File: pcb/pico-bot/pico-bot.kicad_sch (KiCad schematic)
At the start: 27 parts

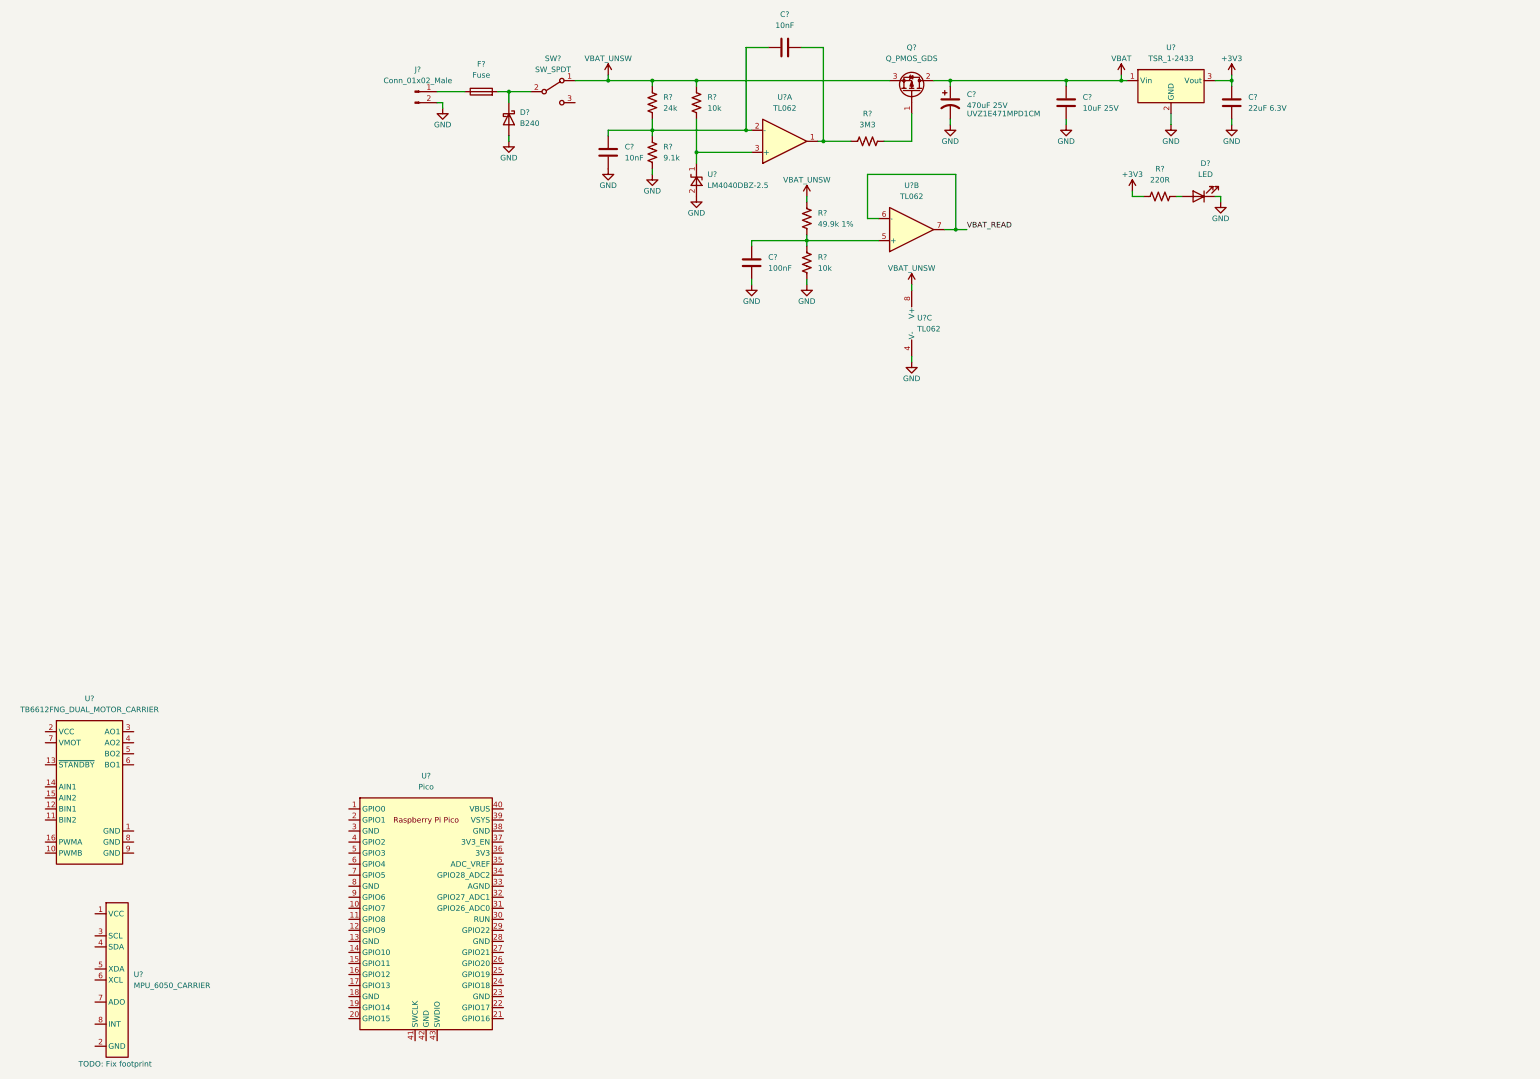
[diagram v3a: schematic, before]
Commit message: Add motor controller and imu circuits, create rpi pico w
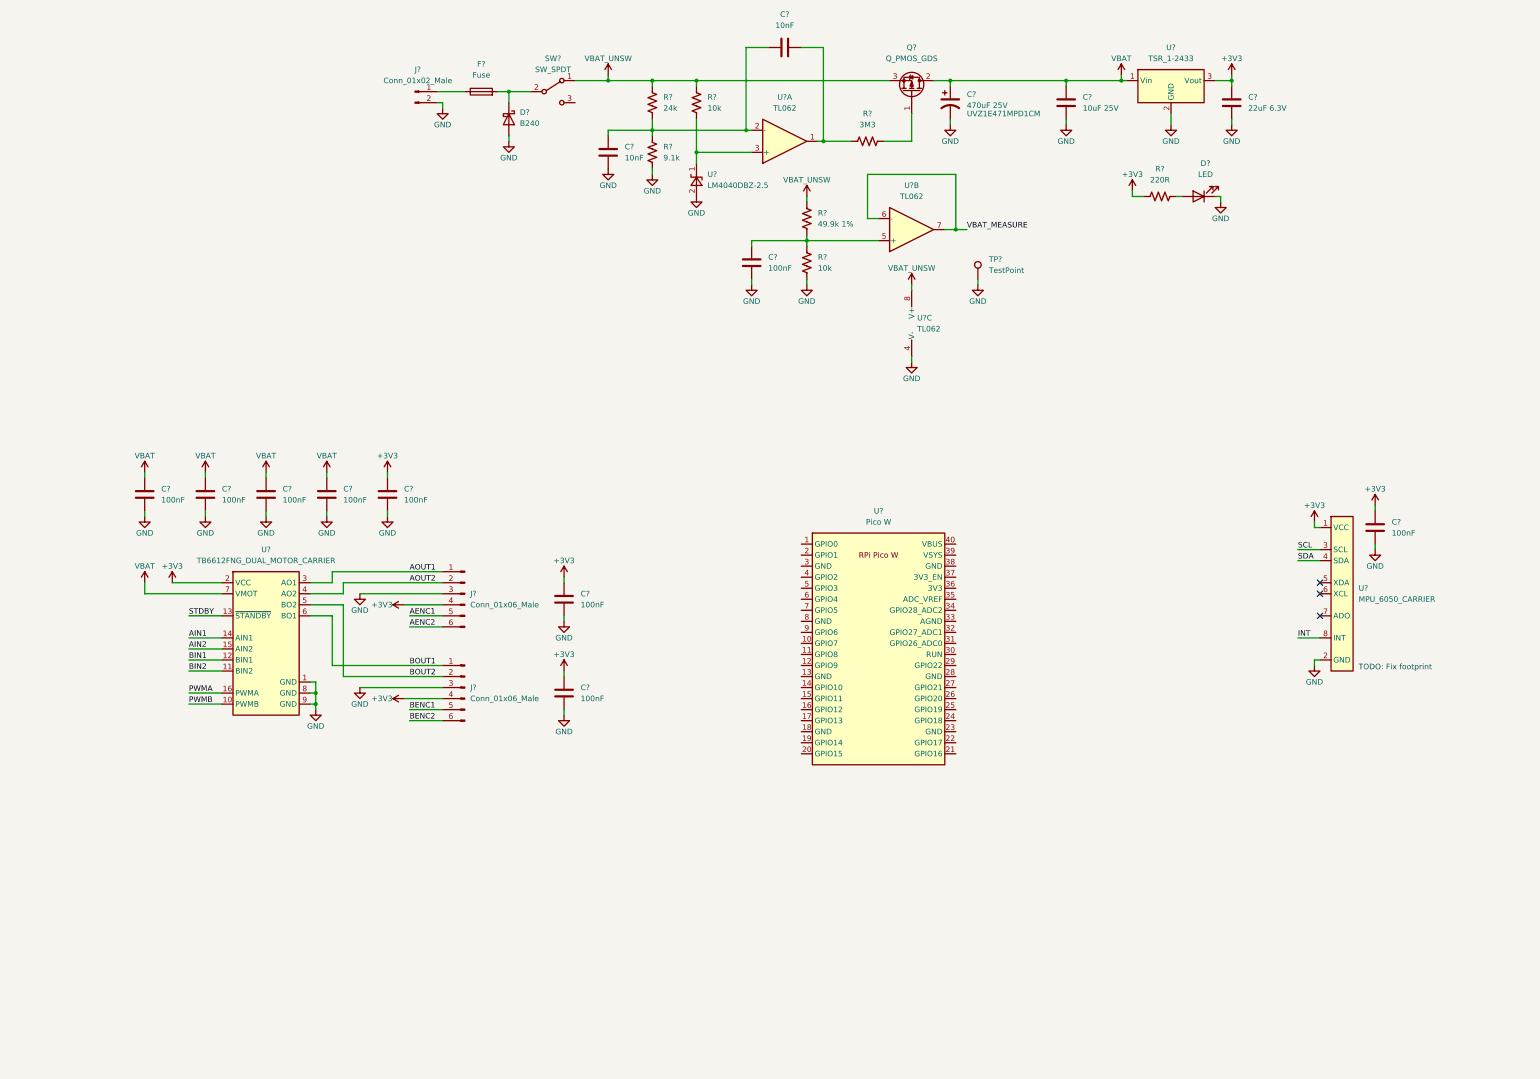
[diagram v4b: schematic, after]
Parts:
- removed U?: Pico, RPi_Pico:RPi_Pico_SMD_TH, symbol MCU_RaspberryPi_and_Boards:Pico
- added C? (x8): 100nF, Capacitor_SMD:C_0805_2012Metric_Pad1.18x1.45mm_HandSolder, symbol Device:C
- added J? (x2): Conn_01x06_Male, Connector_PinHeader_2.54mm:PinHeader_1x06_P2.54mm_Vertical, symbol Connector:Conn_01x06_Male
- added TP?: TestPoint, Connector_PinHeader_2.54mm:PinHeader_1x01_P2.54mm_Vertical, symbol Connector:TestPoint
- added U?: Pico W, RPi_Pico:RPi_Pico_SMD_TH, symbol pico-bot:Pico W
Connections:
- net +3V3: now also U?.1 (VCC), U?.2 (VCC), C?.2, C?.2, C?.2, C?.2, J?.4 (Pin_4), J?.4 (Pin_4)
- net GND: now also U?.1 (GND), U?.2 (GND), U?.8 (GND), U?.9 (GND), C?.1, C?.1, C?.1, C?.1, C?.1, C?.1, C?.1, C?.1, J?.3 (Pin_3), J?.3 (Pin_3), TP?.1
- net VBAT: now also U?.7 (VMOT), C?.2, C?.2, C?.2, C?.2
- net PWMB: now reaches U?.10 (PWMB)
- net BIN2: now reaches U?.11 (BIN2)
- net BIN1: now reaches U?.12 (BIN1)
- net STDBY: now reaches U?.13 (~{STANDBY})
- net AIN1: now reaches U?.14 (AIN1)
- net AIN2: now reaches U?.15 (AIN2)
- net PWMA: now reaches U?.16 (PWMA)
- net AOUT1: now reaches U?.3 (AO1)
- net AOUT1: now also J?.1 (Pin_1)
- net AOUT2: now reaches U?.4 (AO2)
- net AOUT2: now also J?.2 (Pin_2)
- net BOUT2: now reaches U?.5 (BO2)
- net BOUT2: now also J?.2 (Pin_2)
- net BOUT1: now reaches U?.6 (BO1)
- net BOUT1: now also J?.1 (Pin_1)
- net SCL: now reaches U?.3 (SCL)
- net SDA: now reaches U?.4 (SDA)
- net INT: now reaches U?.8 (INT)
- net VBAT_READ renamed VBAT_MEASURE
- new net AENC1: J?.5 (Pin_5)
- new net AENC2: J?.6 (Pin_6)
- new net BENC1: J?.5 (Pin_5)
- new net BENC2: J?.6 (Pin_6)
- no-connect marks 0 -> 3
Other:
- moved on the sheet: U?

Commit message: Progress commit
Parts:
- added Q?: DMG2305UX, symbol Device:Q_PMOS_DGS
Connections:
- net GND: now also U?.13 (GND), U?.18 (GND), U?.23 (GND), U?.28 (GND), U?.3 (GND), U?.33 (AGND), U?.38 (GND), U?.8 (GND)
- net INT: now also U?.11 (GPIO8)
- net SCL: now also U?.10 (GPIO7)
- net SDA: now also U?.9 (GPIO6)
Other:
- note added: "TODO: Check pins match footprint"
- moved on the sheet: C?, J?, U?

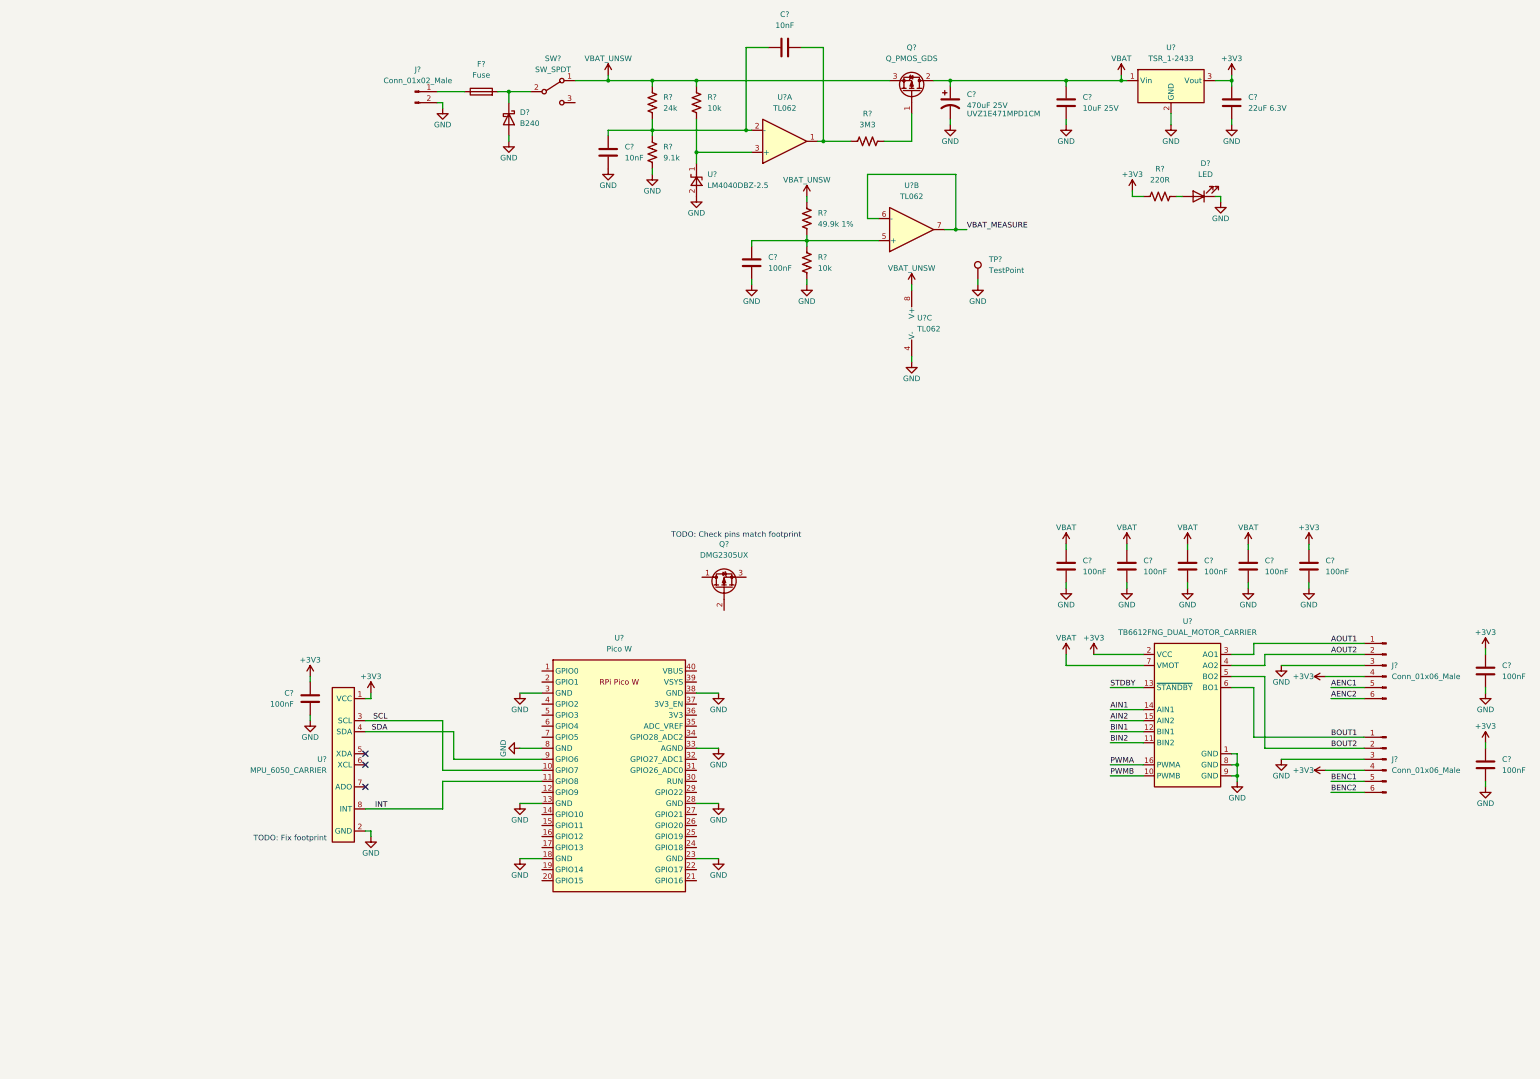
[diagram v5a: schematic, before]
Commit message: Add pico external power circuit, wire up pico
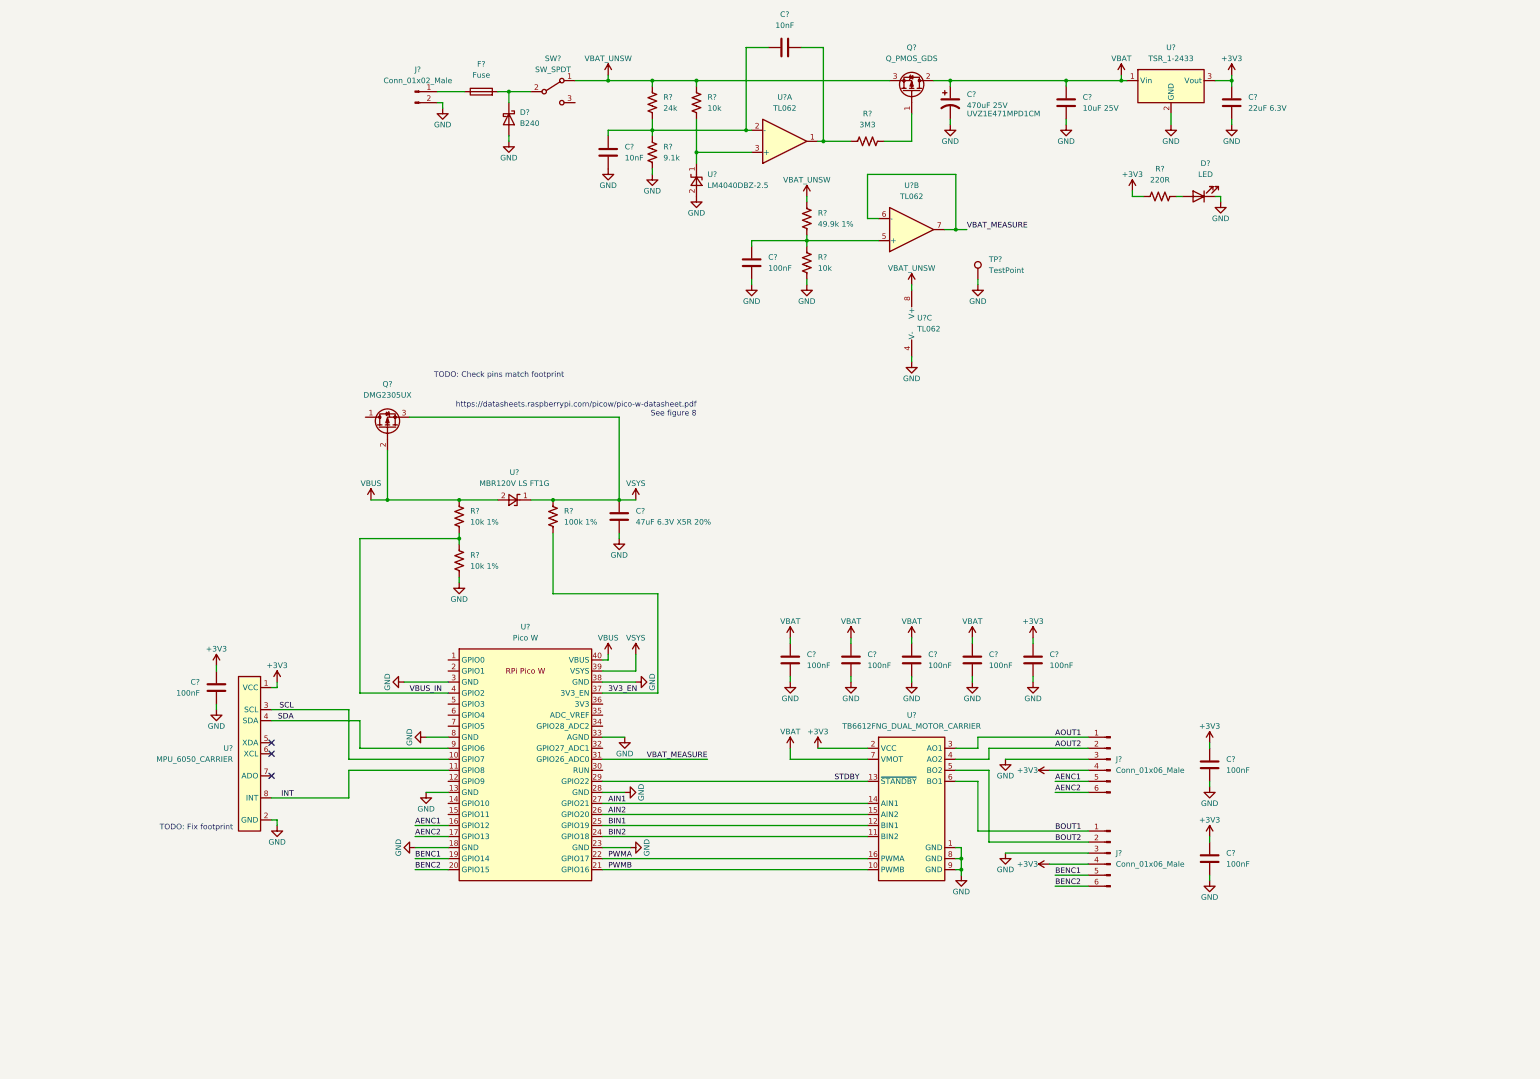
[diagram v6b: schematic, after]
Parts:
- added C?: 47uF 6.3V X5R 20%, Capacitor_SMD:C_0805_2012Metric_Pad1.18x1.45mm_HandSolder, symbol Device:C
- added R? (x2): 10k 1%, Resistor_SMD:R_0805_2012Metric_Pad1.20x1.40mm_HandSolder, symbol Device:R_US
- added R?: 100k 1%, Resistor_SMD:R_0805_2012Metric_Pad1.20x1.40mm_HandSolder, symbol Device:R_US
- added U?: MBR120V LS FT1G, Diode_SMD:D_SOD-123F, symbol Reference_Voltage:LM4040DBZ-2.5
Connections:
- net AENC1: now also U?.16 (GPIO12)
- net AENC2: now also U?.17 (GPIO13)
- net AIN1: now also U?.27 (GPIO21)
- net AIN2: now also U?.26 (GPIO20)
- net BENC1: now also U?.19 (GPIO14)
- net BENC2: now also U?.20 (GPIO15)
- net BIN1: now also U?.25 (GPIO19)
- net BIN2: now also U?.24 (GPIO18)
- net GND: now also C?.1, R?.1
- net PWMA: now also U?.22 (GPIO17)
- net PWMB: now also U?.21 (GPIO16)
- net STDBY: now also U?.29 (GPIO22)
- net VBAT_MEASURE: now also U?.31 (GPIO26_ADC0)
- net VBUS: now reaches Q?.2 (G)
- net VBUS: now also U?.40 (VBUS), R?.2, U?.2 (A)
- net VSYS: now reaches Q?.3 (S)
- net VSYS: now also U?.39 (VSYS), C?.2, R?.2, U?.1 (K)
- net 3V3_EN: now reaches U?.37 (3V3_EN)
- net 3V3_EN: now also R?.1
- net VBUS_IN: now reaches U?.4 (GPIO2)
- net VBUS_IN: now also R?.1, R?.2
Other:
- note added: "https://datasheets.raspberrypi.com/picow/pico-w-datasheet.pdf See figure 8"
- moved on the sheet: C?, J?, Q?, U?

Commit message: Add sw, rgb, update footprints
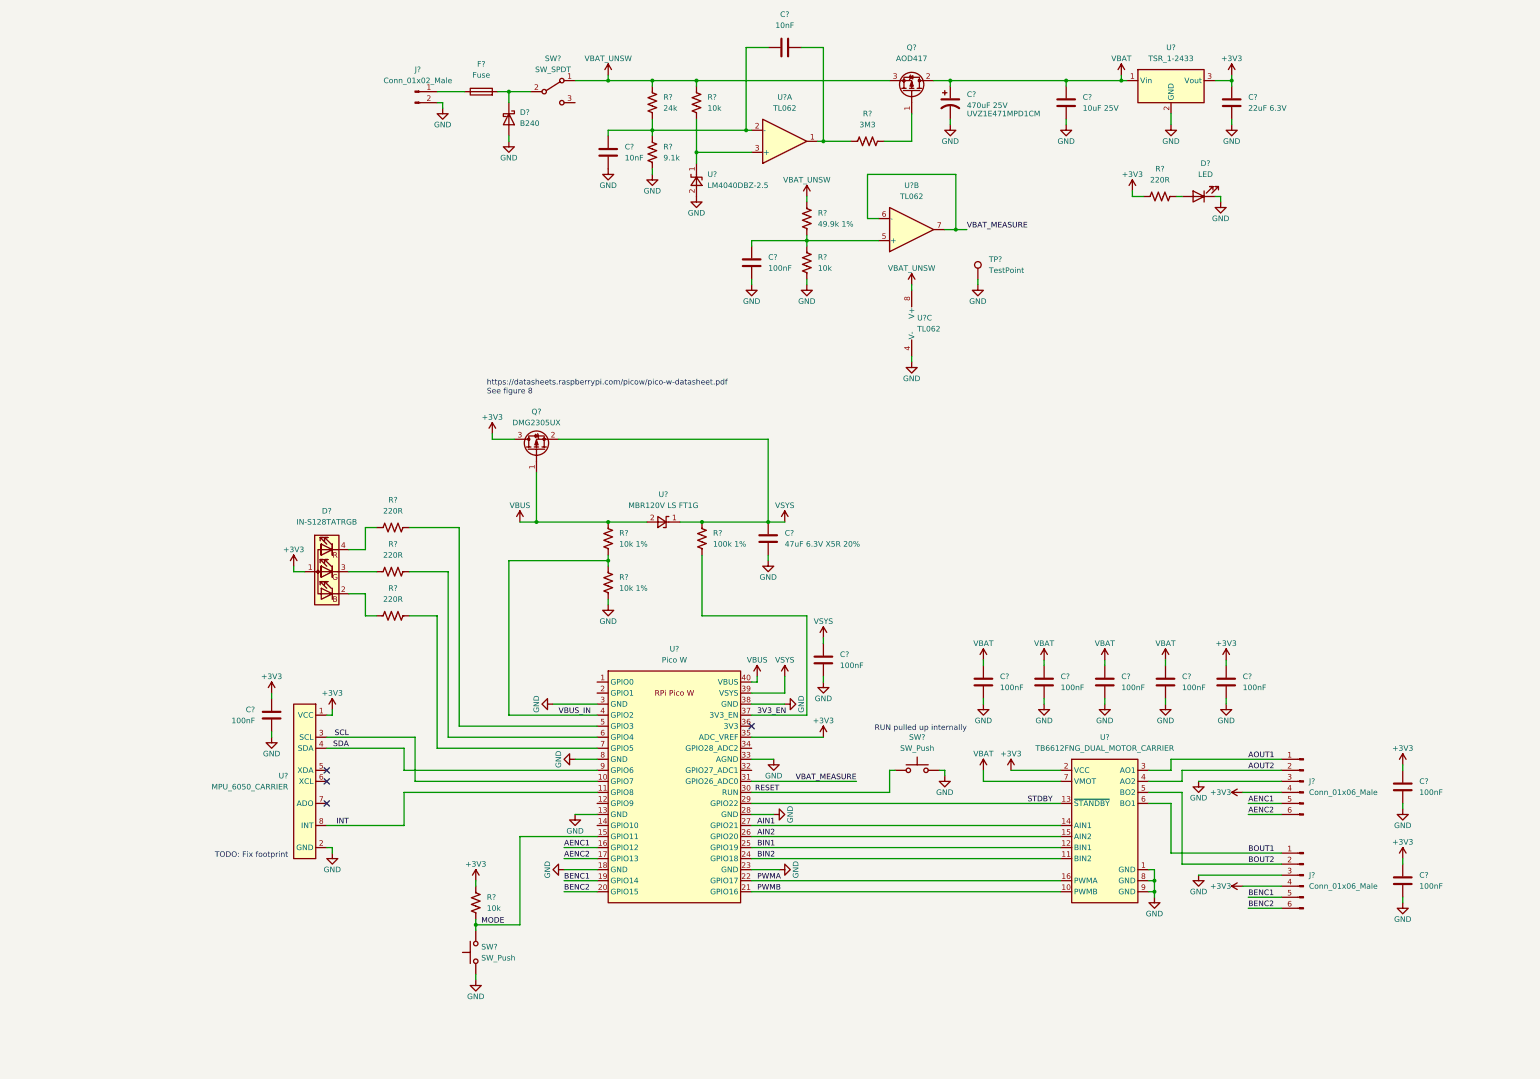
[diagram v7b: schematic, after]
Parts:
- added C?: 100nF, Capacitor_SMD:C_0805_2012Metric_Pad1.18x1.45mm_HandSolder, symbol Device:C
- added D?: IN-S128TATRGB, LED_SMD:LED_RGB_1210, symbol Device:LED_ABGR
- added R? (x3): 220R, Resistor_SMD:R_0805_2012Metric_Pad1.20x1.40mm_HandSolder, symbol Device:R_US
- added R?: 10k, Resistor_SMD:R_0805_2012Metric_Pad1.20x1.40mm_HandSolder, symbol Device:R_US
- added SW? (x2): SW_Push, Button_Switch_THT:SW_PUSH_6mm, symbol Switch:SW_Push
- Q?: footprint (none) -> Package_TO_SOT_SMD:SOT-23
- Q?: value Q_PMOS_GDS -> AOD417; footprint (none) -> Package_TO_SOT_SMD:TO-252-2
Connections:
- net +3V3: now also Q?.3 (D), U?.35 (ADC_VREF), D?.1 (A), R?.2
- net GND: now also C?.1, SW?.1, SW?.2
- net VBUS: now also Q?.1 (G); no longer Q?.2 (G)
- net VSYS: now also Q?.2 (S), C?.2; no longer Q?.3 (S)
- net MODE: now reaches U?.15 (GPIO11)
- net MODE: now also R?.1, SW?.2
- net RESET: now reaches U?.30 (RUN)
- net RESET: now also SW?.1
- net at U?.5 (GPIO3): now also R?.2
- net at U?.6 (GPIO4): now also R?.2
- net at U?.7 (GPIO5): now also R?.2
- new net: D?.2 (BK), R?.1
- new net: D?.3 (GK), R?.1
- new net: D?.4 (RK), R?.1
- no-connect marks 3 -> 4
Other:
- note added: "RUN pulled up internally"
- note removed: "TODO: Check pins match footprint"
- moved on the sheet: C?, J?, Q?, R?, U?
